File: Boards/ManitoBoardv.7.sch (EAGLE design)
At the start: 44 parts, among them U1 BLUETOOTH-RN41", U2 ATMEGA328P

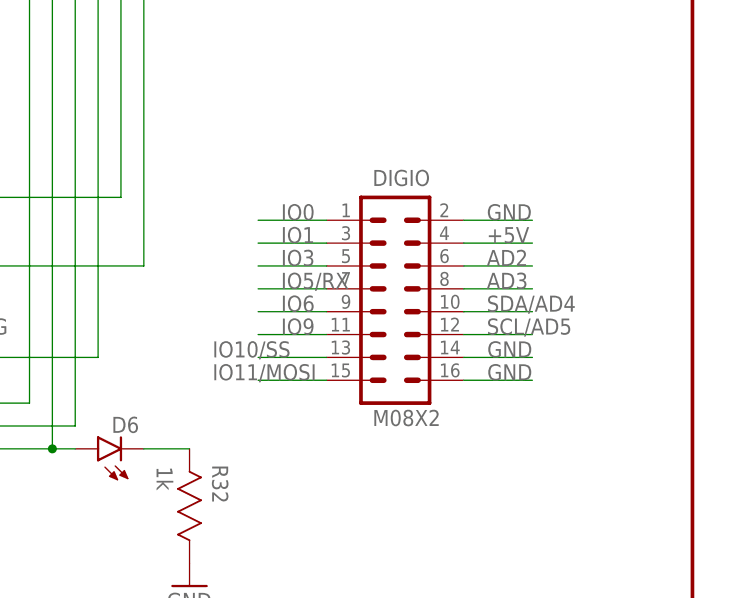
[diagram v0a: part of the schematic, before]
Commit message: IncompleteRevisions
Attempting to shrink board size, reduce variety of trace widths,
simplify angles, remove curved corners, improve thermal relief
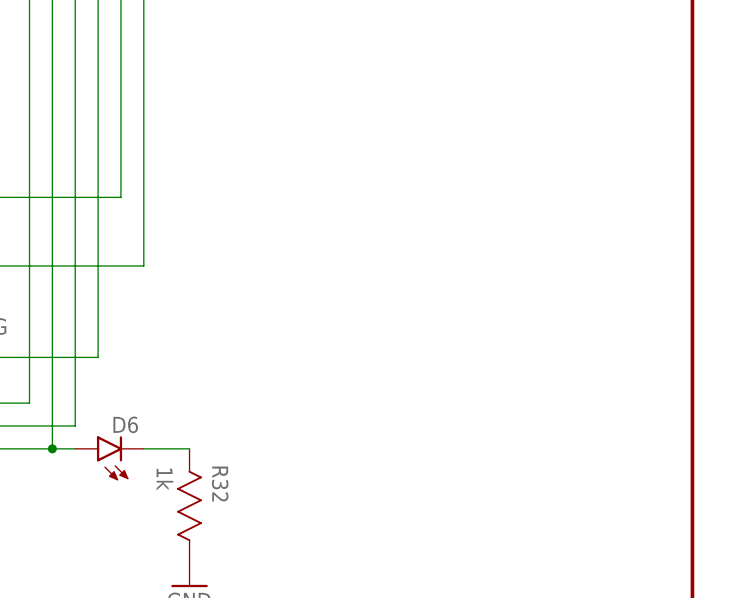
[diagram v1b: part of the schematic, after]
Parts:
- removed DIGIO: M08X2, CharlieCreations:M08X2
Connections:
- net +5V: no longer DIGIO.4
- net AD2: no longer DIGIO.6
- net AD3: no longer DIGIO.8
- net GND: no longer DIGIO.14, DIGIO.16, DIGIO.2
- net IO0: no longer DIGIO.1
- net IO1: no longer DIGIO.3
- net IO10/SS: no longer DIGIO.13
- net IO11/MOSI: no longer DIGIO.15
- net IO3: no longer DIGIO.5
- net IO5/RX: no longer DIGIO.7
- net IO6: no longer DIGIO.9
- net IO9: no longer DIGIO.11
- net SCL/AD5: no longer DIGIO.12
- net SDA/AD4: no longer DIGIO.10
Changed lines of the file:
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@@
 <?xml version="1.0" encoding="utf-8"?>
 <!DOCTYPE eagle SYSTEM "eagle.dtd">
-<eagle version="7.2.0">
+<eagle version="7.1.0">
 <drawing>
 <settings>
@@
 <part name="5V" library="CharlieCreations" deviceset="M01" device="SPRING-CONN"/>
 <part name="R30" library="CharlieCreations" deviceset="0603RESISTOR" device="1" value="10k"/>
-<part name="DIGIO" library="CharlieCreations" deviceset="M08X2" device=""/>
 <part name="R32" library="CharlieCreations" deviceset="0603RESISTOR" device="1" value="1k"/>
 <part name="U$1" library="CharlieCreations" deviceset="VSK-S3-5U" device="1"/>
@@
 </instance>
 <instance part="R30" gate="A" x="99.06" y="182.88" rot="R270"/>
-<instance part="DIGIO" gate="G$1" x="233.68" y="127"/>
 <instance part="R32" gate="A" x="210.82" y="111.76" rot="R270"/>
 <instance part="U$1" gate="G$1" x="223.52" y="373.38"/>
@@
 </segment>
 <segment>
-<wire x1="248.92" y1="137.16" x2="241.3" y2="137.16" width="0.1524" layer="91"/>
-<label x="243.84" y="137.16" size="1.778" layer="95"/>
-<pinref part="DIGIO" gate="G$1" pin="2"/>
-</segment>
-<segment>
-<wire x1="241.3" y1="121.92" x2="248.92" y2="121.92" width="0.1524" layer="91"/>
-<label x="248.92" y="123.698" size="1.778" layer="95" rot="R180"/>
-<pinref part="DIGIO" gate="G$1" pin="14"/>
-</segment>
-<segment>
 <pinref part="GND10" gate="1" pin="GND"/>
 <pinref part="R32" gate="A" pin="1"/>
@@
 <wire x1="264.16" y1="386.08" x2="264.16" y2="383.54" width="0.1524" layer="91"/>
 <junction x="254" y="386.08"/>
-</segment>
-<segment>
-<wire x1="241.3" y1="119.38" x2="248.92" y2="119.38" width="0.1524" layer="91"/>
-<label x="248.92" y="121.158" size="1.778" layer="95" rot="R180"/>
-<pinref part="DIGIO" gate="G$1" pin="16"/>
 </segment>
 <segment>
@@
 <junction x="99.06" y="185.42"/>
 <pinref part="D1" gate="G$1" pin="C"/>
-</segment>
-<segment>
-<wire x1="248.92" y1="134.62" x2="241.3" y2="134.62" width="0.1524" layer="91"/>
-<label x="243.84" y="134.62" size="1.778" layer="95"/>
-<pinref part="DIGIO" gate="G$1" pin="4"/>
 </segment>
 <segment>
@@
 <label x="177.8" y="144.78" size="1.778" layer="95"/>
 </segment>
-<segment>
-<wire x1="226.06" y1="134.62" x2="218.44" y2="134.62" width="0.1524" layer="91"/>
-<label x="220.98" y="134.62" size="1.778" layer="95"/>
-<pinref part="DIGIO" gate="G$1" pin="3"/>
-</segment>
 </net>
 <net name="IO0" class="0">
@@
 <wire x1="182.88" y1="147.32" x2="175.26" y2="147.32" width="0.1524" layer="91"/>
 <label x="177.8" y="147.32" size="1.778" layer="95"/>
-</segment>
-<segment>
-<wire x1="226.06" y1="137.16" x2="218.44" y2="137.16" width="0.1524" layer="91"/>
-<label x="220.98" y="137.16" size="1.778" layer="95"/>
-<pinref part="DIGIO" gate="G$1" pin="1"/>
 </segment>
 </net>
@@
 <label x="154.94" y="195.58" size="1.778" layer="95"/>
 <label x="177.8" y="116.84" size="1.778" layer="95"/>
-</segment>
-<segment>
-<wire x1="226.06" y1="119.38" x2="218.44" y2="119.38" width="0.1524" layer="91"/>
-<label x="213.36" y="119.38" size="1.778" layer="95"/>
-<pinref part="DIGIO" gate="G$1" pin="15"/>
 </segment>
 <segment>
@@
 <wire x1="177.8" y1="213.36" x2="180.34" y2="213.36" width="0.1524" layer="91"/>
 </segment>
-<segment>
-<wire x1="226.06" y1="127" x2="218.44" y2="127" width="0.1524" layer="91"/>
-<label x="220.98" y="127" size="1.778" layer="95"/>
-<pinref part="DIGIO" gate="G$1" pin="9"/>
-</segment>
 </net>
 <net name="IO3" class="0">
@@
 <wire x1="203.2" y1="139.7" x2="175.26" y2="139.7" width="0.1524" layer="91"/>
 </segment>
-<segment>
-<wire x1="226.06" y1="132.08" x2="218.44" y2="132.08" width="0.1524" layer="91"/>
-<label x="220.98" y="132.08" size="1.778" layer="95"/>
-<pinref part="DIGIO" gate="G$1" pin="5"/>
-</segment>
 </net>
 <net name="IO5/RX" class="0">
-<segment>
-<wire x1="226.06" y1="129.54" x2="218.44" y2="129.54" width="0.1524" layer="91"/>
-<label x="220.98" y="129.54" size="1.778" layer="95"/>
-<pinref part="DIGIO" gate="G$1" pin="7"/>
-</segment>
 <segment>
 <label x="35.56" y="45.72" size="1.778" layer="95"/>
@@
 </net>
 <net name="IO9" class="0">
-<segment>
-<wire x1="226.06" y1="124.46" x2="218.44" y2="124.46" width="0.1524" layer="91"/>
-<label x="220.98" y="124.46" size="1.778" layer="95"/>
-<pinref part="DIGIO" gate="G$1" pin="11"/>
-</segment>
 <segment>
 <label x="177.8" y="121.92" size="1.778" layer="95"/>
@@
 </segment>
 <segment>
-<wire x1="226.06" y1="121.92" x2="218.44" y2="121.92" width="0.1524" layer="91"/>
-<label x="213.36" y="121.92" size="1.778" layer="95"/>
-<pinref part="DIGIO" gate="G$1" pin="13"/>
-</segment>
-<segment>
 <pinref part="JP1" gate="G$1" pin="6"/>
 <wire x1="203.2" y1="60.96" x2="218.44" y2="60.96" width="0.1524" layer="91"/>
@@
 <label x="177.8" y="162.56" size="1.778" layer="95"/>
 </segment>
-<segment>
-<wire x1="248.92" y1="129.54" x2="241.3" y2="129.54" width="0.1524" layer="91"/>
-<label x="243.84" y="129.54" size="1.778" layer="95"/>
-<pinref part="DIGIO" gate="G$1" pin="8"/>
-</segment>
 </net>
 <net name="AD2" class="0">
@@
 <label x="177.8" y="165.1" size="1.778" layer="95"/>
 </segment>
-<segment>
-<wire x1="248.92" y1="132.08" x2="241.3" y2="132.08" width="0.1524" layer="91"/>
-<label x="243.84" y="132.08" size="1.778" layer="95"/>
-<pinref part="DIGIO" gate="G$1" pin="6"/>
-</segment>
 </net>
 <net name="AD1" class="0">
@@
 <wire x1="175.26" y1="160.02" x2="180.34" y2="160.02" width="0.1524" layer="91"/>
 </segment>
-<segment>
-<wire x1="248.92" y1="127" x2="241.3" y2="127" width="0.1524" layer="91"/>
-<label x="243.84" y="127" size="1.778" layer="95"/>
-<pinref part="DIGIO" gate="G$1" pin="10"/>
-</segment>
 </net>
 <net name="SCL/AD5" class="0">
 <segment>
-<wire x1="248.92" y1="124.46" x2="241.3" y2="124.46" width="0.1524" layer="91"/>
-<label x="243.84" y="124.46" size="1.778" layer="95"/>
-<pinref part="DIGIO" gate="G$1" pin="12"/>
-</segment>
-<segment>
 <pinref part="U2" gate="G$1" pin="PC5(ADC5/SCL)"/>
